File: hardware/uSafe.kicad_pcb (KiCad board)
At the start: 2 copper layers, 63.5 x 88.9 mm, 8 parts, among them Q1 BUZ11

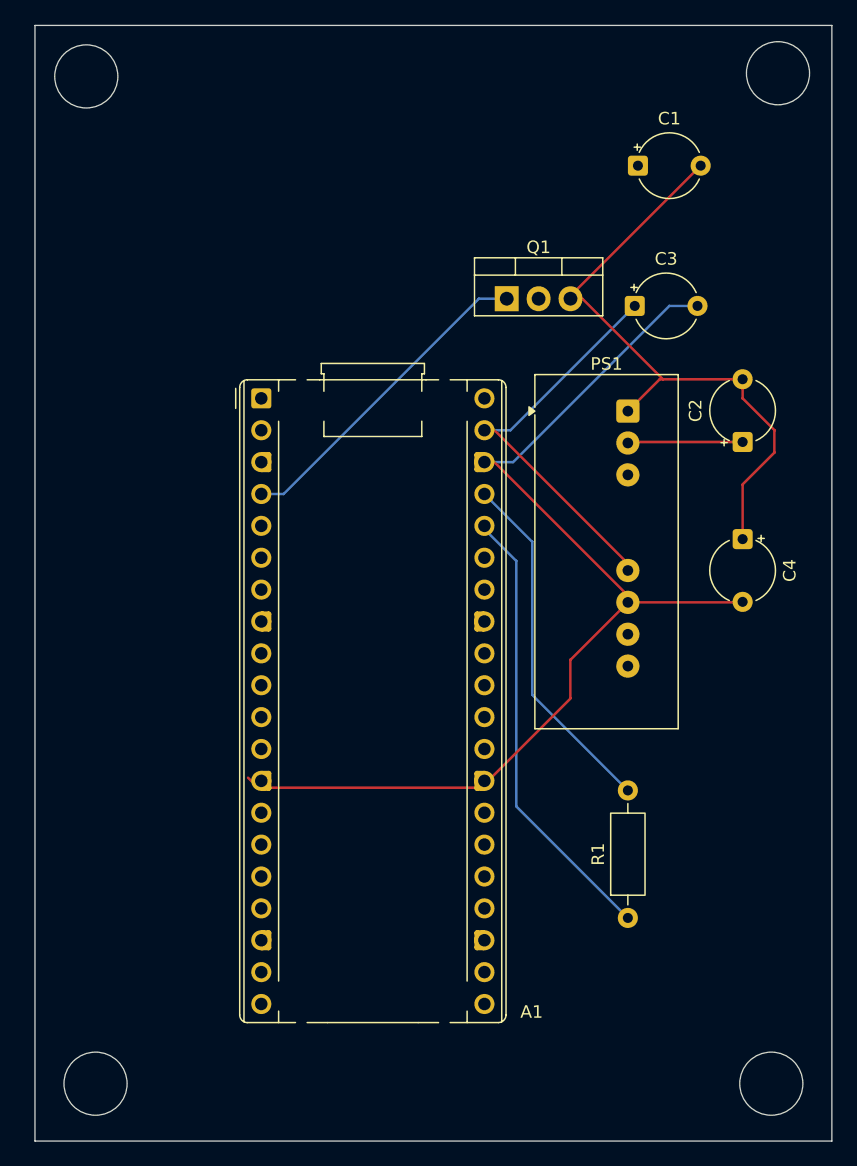
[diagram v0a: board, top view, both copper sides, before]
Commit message: added keypad connector
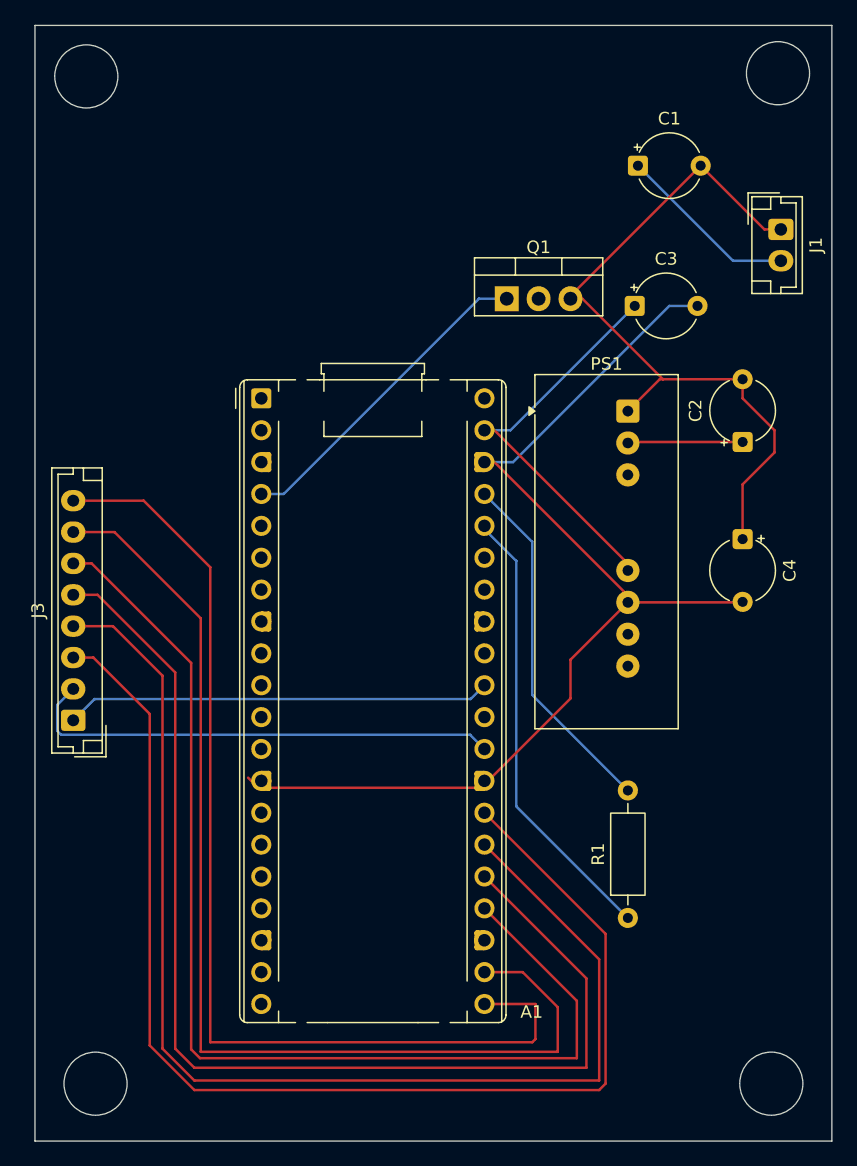
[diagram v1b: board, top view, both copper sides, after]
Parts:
- added J1: Conn_01x02_Socket, Connector_JST:JST_EH_B2B-EH-A_1x02_P2.50mm_Vertical, F.Cu at (173.7, 80.0)
- added J3: Conn_01x08_Pin, Connector_JST:JST_EH_B8B-EH-A_1x08_P2.50mm_Vertical, F.Cu at (117.3, 119.1)
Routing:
- net Net-(A1-GPIO21): track 0.00 -> 98.0 mm
- net Net-(A1-GPIO20): track 0.00 -> 96.9 mm
- net Net-(A1-GPIO19): track 0.00 -> 92.7 mm
- net Net-(A1-GPIO18): track 0.00 -> 89.5 mm
- net Net-(A1-GPIO17): track 0.00 -> 86.6 mm
- net Net-(A1-GPIO16): track 0.00 -> 83.8 mm
- net Net-(A1-GPIO22): track 0.00 -> 38.5 mm
- net Net-(A1-GPIO26_ADC0): track 0.00 -> 33.9 mm
- net Net-(J1-Pin_2): track 0.00 -> 14.5 mm
- net Net-(J1-Pin_1): track 50.0 -> 58.5 mm
